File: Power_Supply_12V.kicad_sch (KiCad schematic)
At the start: 14 parts, among them J4 -12V, J5 GND, J6 +12V, U1 LM7812_TO220, U2 LM7912_TO220

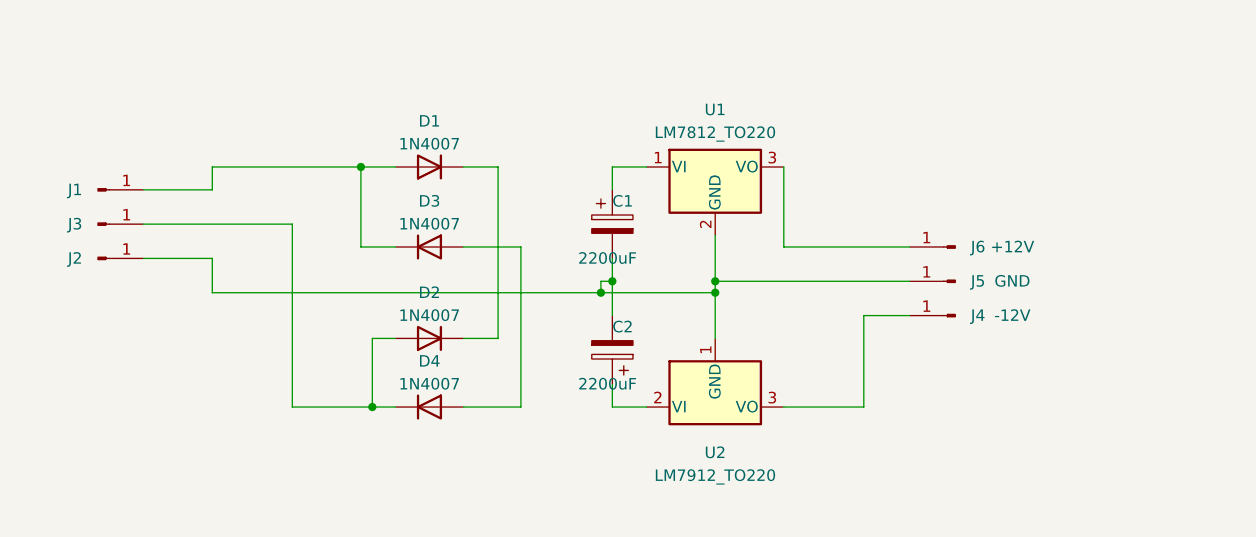
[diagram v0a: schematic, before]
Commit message: Added components and footprints
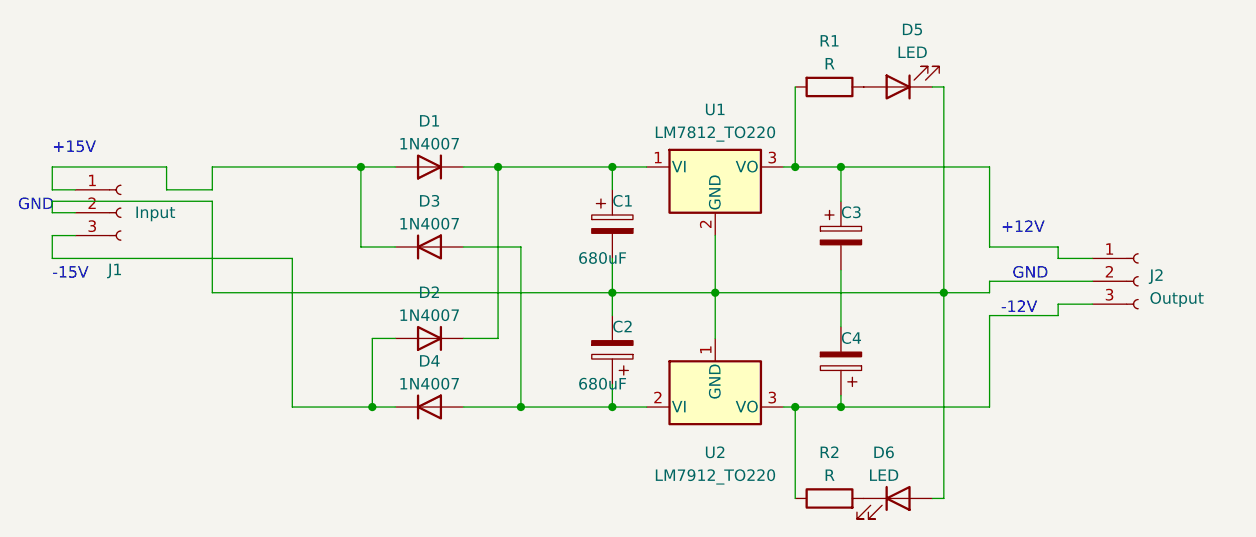
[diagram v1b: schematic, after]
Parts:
- removed J1, J2, J3: ~, Connector_PinHeader_1.00mm:PinHeader_1x01_P1.00mm_Vertical, symbol Connector:Conn_01x01_Pin
- removed J4: -12V, Connector_PinHeader_1.00mm:PinHeader_1x01_P1.00mm_Vertical, symbol Connector:Conn_01x01_Pin
- removed J5: GND, Connector_PinHeader_1.00mm:PinHeader_1x01_P1.00mm_Vertical, symbol Connector:Conn_01x01_Pin
- removed J6: +12V, Connector_PinHeader_1.00mm:PinHeader_1x01_P1.00mm_Vertical, symbol Connector:Conn_01x01_Pin
- added C3, C4: ~, Capacitor_THT:CP_Radial_D4.0mm_P1.50mm, symbol Device:C_Polarized
- added D5, D6: LED, LED_THT:LED_D3.0mm, symbol Device:LED
- added J1: Input, TerminalBlock_Phoenix:TerminalBlock_Phoenix_MKDS-1,5-3-5.08_1x03_P5.08mm_Horizontal, symbol Connector:Conn_01x03_Socket
- added J2: Output, TerminalBlock_Phoenix:TerminalBlock_Phoenix_MKDS-1,5-3-5.08_1x03_P5.08mm_Horizontal, symbol Connector:Conn_01x03_Socket
- added R1, R2: R, Resistor_THT:R_Axial_DIN0204_L3.6mm_D1.6mm_P5.08mm_Horizontal, symbol Device:R
- C1, C2: value 2200uF -> 680uF
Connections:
- net at D1.2 (A), D3.1 (K): now also J1.1 (Pin_1)
- net at D3.2 (A), D4.2 (A): now also C2.1, U2.2 (VI)
- net at D2.2 (A), D4.1 (K): now also J1.3 (Pin_3)
- net at C1.2, C2.2, U1.2 (GND)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: now also D5.1 (K), D6.2 (A), J1.2 (Pin_2), J2.2 (Pin_2)
- net at U1.3 (VO): now also C3.1, J2.1 (Pin_1), R1.2
- net at D1.1 (K), D2.1 (K): now also C1.1, U1.1 (VI)
- net at U2.3 (VO): now also C4.1, J2.3 (Pin_3), R2.1
- new net: D6.1 (K), R2.2
- new net: D5.2 (A), R1.1
- new net: C3.2, C4.2
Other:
- note added: "+12V"
- note added: "+15V"
- note added: "-12V"
- note added: "-15V"
- note added: "GND"

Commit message: Routing done
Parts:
- C1, C2, C3, C4: footprint Capacitor_THT:CP_Radial_D4.0mm_P1.50mm -> Capacitor_THT:CP_Radial_D10.0mm_P5.00mm
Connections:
- net at C4.1, R2.1, U2.3 (VO): now also J2.1 (Pin_1); no longer J2.3 (Pin_3)
- net at C1.2, C2.2, D5.1 (K)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: now also C3.2, C4.2
- net at C3.1, R1.2, U1.3 (VO): now also J2.3 (Pin_3); no longer J2.1 (Pin_1)
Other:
- moved on the sheet: J2
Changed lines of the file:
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@@
   (junction (at 151.13 99.06) (diameter 0) (color 0 0 0 0)
   )
+  (junction (at 176.53 113.03) (diameter 0) (color 0 0 0 0)
+  )
   (junction (at 124.46 125.73) (diameter 0) (color 0 0 0 0)
   )
@@
   (junction (at 171.45 99.06) (diameter 0) (color 0 0 0 0)
   )
-  (wire (pts (xy 193.04 115.57) (xy 200.66 115.57))
-    (stroke (width 0) (type default))
-  )
   (wire (pts (xy 140.97 107.95) (xy 140.97 125.73))
     (stroke (width 0) (type default))
@@
     (stroke (width 0) (type default))
   )
-  (wire (pts (xy 200.66 109.22) (xy 204.47 109.22))
-    (stroke (width 0) (type default))
-  )
   (wire (pts (xy 88.9 106.68) (xy 91.44 106.68))
     (stroke (width 0) (type default))
@@
     (stroke (width 0) (type default))
   )
+  (wire (pts (xy 213.36 113.03) (xy 213.36 111.76))
+    (stroke (width 0) (type default))
+  )
   (wire (pts (xy 123.19 107.95) (xy 127 107.95))
     (stroke (width 0) (type default))
@@
     (stroke (width 0) (type default))
   )
+  (wire (pts (xy 176.53 113.03) (xy 187.96 113.03))
+    (stroke (width 0) (type default))
+  )
   (wire (pts (xy 176.53 124.46) (xy 176.53 125.73))
     (stroke (width 0) (type default))
@@
     (stroke (width 0) (type default))
   )
-  (wire (pts (xy 193.04 107.95) (xy 200.66 107.95))
-    (stroke (width 0) (type default))
-  )
-  (wire (pts (xy 176.53 125.73) (xy 193.04 125.73))
+  (wire (pts (xy 176.53 125.73) (xy 213.36 125.73))
     (stroke (width 0) (type default))
   )
@@
     (stroke (width 0) (type default))
   )
-  (wire (pts (xy 200.66 114.3) (xy 204.47 114.3))
-    (stroke (width 0) (type default))
-  )
   (wire (pts (xy 151.13 109.22) (xy 151.13 113.03))
     (stroke (width 0) (type default))
@@
     (stroke (width 0) (type default))
   )
-  (wire (pts (xy 176.53 99.06) (xy 193.04 99.06))
+  (wire (pts (xy 176.53 99.06) (xy 213.36 99.06))
     (stroke (width 0) (type default))
   )
@@
     (stroke (width 0) (type default))
   )
-  (wire (pts (xy 176.53 110.49) (xy 176.53 116.84))
-    (stroke (width 0) (type default))
-  )
   (wire (pts (xy 138.43 99.06) (xy 138.43 118.11))
     (stroke (width 0) (type default))
   )
-  (wire (pts (xy 200.66 115.57) (xy 200.66 114.3))
-    (stroke (width 0) (type default))
-  )
   (wire (pts (xy 115.57 109.22) (xy 88.9 109.22))
     (stroke (width 0) (type default))
   )
+  (wire (pts (xy 213.36 114.3) (xy 210.82 114.3))
+    (stroke (width 0) (type default))
+  )
   (wire (pts (xy 151.13 113.03) (xy 151.13 115.57))
     (stroke (width 0) (type default))
@@
     (stroke (width 0) (type default))
   )
+  (wire (pts (xy 213.36 99.06) (xy 213.36 109.22))
+    (stroke (width 0) (type default))
+  )
   (wire (pts (xy 123.19 99.06) (xy 127 99.06))
     (stroke (width 0) (type default))
   )
+  (wire (pts (xy 213.36 125.73) (xy 213.36 114.3))
+    (stroke (width 0) (type default))
+  )
   (wire (pts (xy 106.68 113.03) (xy 151.13 113.03))
     (stroke (width 0) (type default))
@@
     (stroke (width 0) (type default))
   )
-  (wire (pts (xy 193.04 113.03) (xy 193.04 111.76))
+  (wire (pts (xy 176.53 113.03) (xy 176.53 116.84))
     (stroke (width 0) (type default))
   )
@@
     (stroke (width 0) (type default))
   )
-  (wire (pts (xy 193.04 125.73) (xy 193.04 115.57))
-    (stroke (width 0) (type default))
-  )
   (wire (pts (xy 171.45 125.73) (xy 176.53 125.73))
     (stroke (width 0) (type default))
   )
+  (wire (pts (xy 176.53 110.49) (xy 176.53 113.03))
+    (stroke (width 0) (type default))
+  )
   (wire (pts (xy 134.62 107.95) (xy 140.97 107.95))
     (stroke (width 0) (type default))
@@
     (stroke (width 0) (type default))
   )
-  (wire (pts (xy 193.04 111.76) (xy 204.47 111.76))
-    (stroke (width 0) (type default))
-  )
-  (wire (pts (xy 200.66 107.95) (xy 200.66 109.22))
-    (stroke (width 0) (type default))
-  )
-  (wire (pts (xy 162.56 113.03) (xy 187.96 113.03))
+  (wire (pts (xy 162.56 113.03) (xy 176.53 113.03))
     (stroke (width 0) (type default))
   )
@@
     (stroke (width 0) (type default))
   )
+  (wire (pts (xy 187.96 113.03) (xy 213.36 113.03))
+    (stroke (width 0) (type default))
+  )
   (wire (pts (xy 134.62 99.06) (xy 138.43 99.06))
     (stroke (width 0) (type default))
   )
-  (wire (pts (xy 193.04 99.06) (xy 193.04 107.95))
-    (stroke (width 0) (type default))
-  )
   (wire (pts (xy 138.43 99.06) (xy 151.13 99.06))
     (stroke (width 0) (type default))
@@
     (stroke (width 0) (type default))
   )
-  (wire (pts (xy 187.96 113.03) (xy 193.04 113.03))
-    (stroke (width 0) (type default))
-  )
   (wire (pts (xy 140.97 125.73) (xy 134.62 125.73))
     (stroke (width 0) (type default))
@@
     (stroke (width 0) (type default))
   )
+  (wire (pts (xy 213.36 109.22) (xy 210.82 109.22))
+    (stroke (width 0) (type default))
+  )
   (wire (pts (xy 123.19 99.06) (xy 123.19 107.95))
     (stroke (width 0) (type default))
@@
     (stroke (width 0) (type default))
   )
+  (wire (pts (xy 213.36 111.76) (xy 210.82 111.76))
+    (stroke (width 0) (type default))
+  )
   (wire (pts (xy 115.57 125.73) (xy 124.46 125.73))
     (stroke (width 0) (type default))
@@
     (stroke (width 0) (type default))
   )
-  (text "+12V\n" (at 194.31 106.68 0)
+  (text "+12V\n" (at 214.63 109.22 0)
     (effects (font (size 1.27 1.27)) (justify left bottom))
   )
@@
     (effects (font (size 1.27 1.27)) (justify left bottom))
   )
-  (text "GND\n" (at 195.58 111.76 0)
+  (text "GND\n" (at 214.63 113.03 0)
     (effects (font (size 1.27 1.27)) (justify left bottom))
   )
-  (text "-12V" (at 194.31 115.57 0)
+  (text "-12V" (at 214.63 116.84 0)
     (effects (font (size 1.27 1.27)) (justify left bottom))
   )
@@
       (effects (font (size 1.27 1.27)) (justify left))
     )
-    (property "Footprint" "Capacitor_THT:CP_Radial_D4.0mm_P1.50mm" (at 152.0952 109.22 0)
+    (property "Footprint" "Capacitor_THT:CP_Radial_D10.0mm_P5.00mm" (at 152.0952 109.22 0)
       (effects (font (size 1.27 1.27)) hide)
     )
@@
       (effects (font (size 1.27 1.27)) (justify left))
     )
-    (property "Footprint" "Capacitor_THT:CP_Radial_D4.0mm_P1.50mm" (at 177.4952 110.49 0)
+    (property "Footprint" "Capacitor_THT:CP_Radial_D10.0mm_P5.00mm" (at 177.4952 110.49 0)
       (effects (font (size 1.27 1.27)) hide)
     )
@@
     )
   )
-  (symbol (lib_id "Connector:Conn_01x03_Socket") (at 209.55 111.76 0) (unit 1)
-    (in_bom yes) (on_board yes) (dnp no) (fields_autoplaced)
-    (property "Reference" "J2" (at 210.82 111.125 0)
-      (effects (font (size 1.27 1.27)) (justify left))
-    )
-    (property "Value" "Output" (at 210.82 113.665 0)
-      (effects (font (size 1.27 1.27)) (justify left))
-    )
-    (property "Footprint" "TerminalBlock_Phoenix:TerminalBlock_Phoenix_MKDS-1,5-3-5.08_1x03_P5.08mm_Horizontal" (at 209.55 111.76 0)
-      (effects (font (size 1.27 1.27)) hide)
-    )
-    (property "Datasheet" "~" (at 209.55 111.76 0)
+  (symbol (lib_id "Connector:Conn_01x03_Socket") (at 205.74 111.76 180) (unit 1)
+    (in_bom yes) (on_board yes) (dnp no) (fields_autoplaced)
+    (property "Reference" "J2" (at 206.375 105.41 0)
+      (effects (font (size 1.27 1.27)))
+    )
+    (property "Value" "Output" (at 206.375 107.95 0)
+      (effects (font (size 1.27 1.27)))
+    )
+    (property "Footprint" "TerminalBlock_Phoenix:TerminalBlock_Phoenix_MKDS-1,5-3-5.08_1x03_P5.08mm_Horizontal" (at 205.74 111.76 0)
+      (effects (font (size 1.27 1.27)) hide)
+    )
+    (property "Datasheet" "~" (at 205.74 111.76 0)
       (effects (font (size 1.27 1.27)) hide)
     )
@@
       (effects (font (size 1.27 1.27)) (justify right))
     )
-    (property "Footprint" "Capacitor_THT:CP_Radial_D4.0mm_P1.50mm" (at 150.1648 115.57 0)
+    (property "Footprint" "Capacitor_THT:CP_Radial_D10.0mm_P5.00mm" (at 150.1648 115.57 0)
       (effects (font (size 1.27 1.27)) hide)
     )
@@
       (effects (font (size 1.27 1.27)) (justify right))
     )
-    (property "Footprint" "Capacitor_THT:CP_Radial_D4.0mm_P1.50mm" (at 175.5648 116.84 0)
-      (effects (font (size 1.27 1.27)) hide)
-    )
+    (property "Footprint" "Capacitor_THT:CP_Radial_D10.0mm_P5.00mm" (at 175.5648 116.84 0)
+      (effects (font (size 1.27 1.27)) hide)
+    )
